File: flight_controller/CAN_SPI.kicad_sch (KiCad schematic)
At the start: 11 parts, among them CN2 HCZZ0494-4, CN3 HCZZ0494-4, U3 TJA1051TK/3,118, U5 TJA1051TK/3,118, U6 KRCLAMP0521P-N

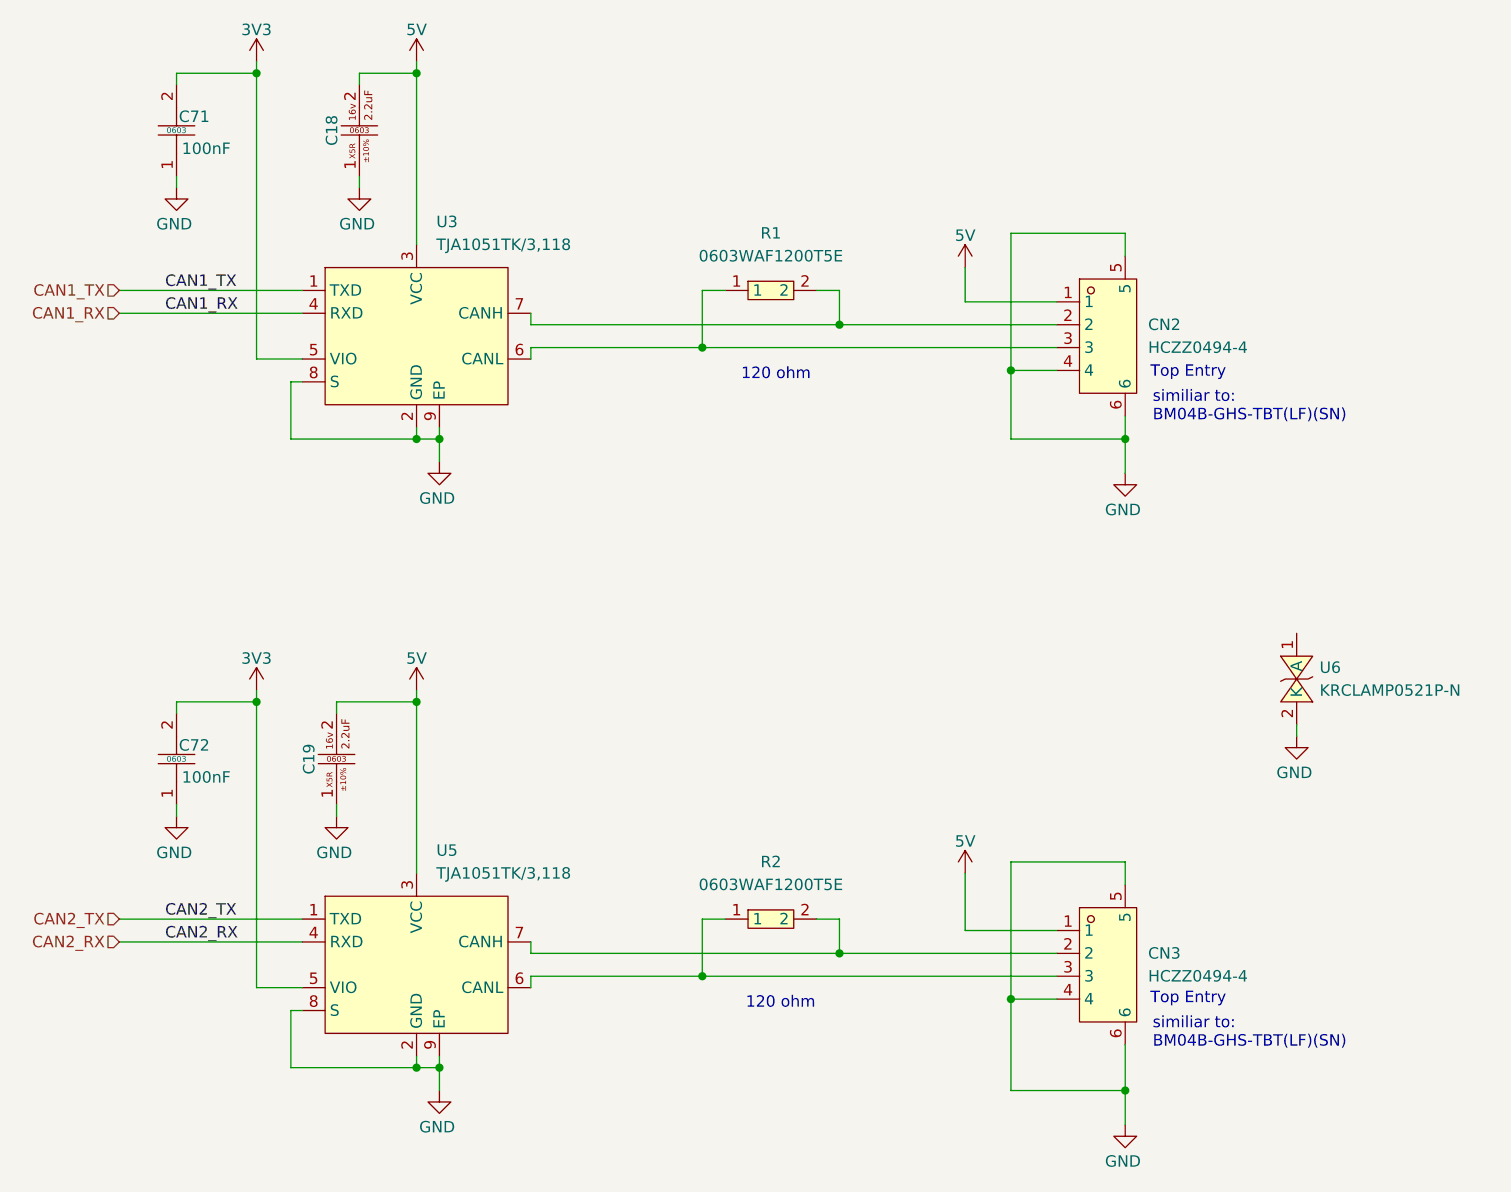
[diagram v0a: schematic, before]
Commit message: updating symbols as in the shared library
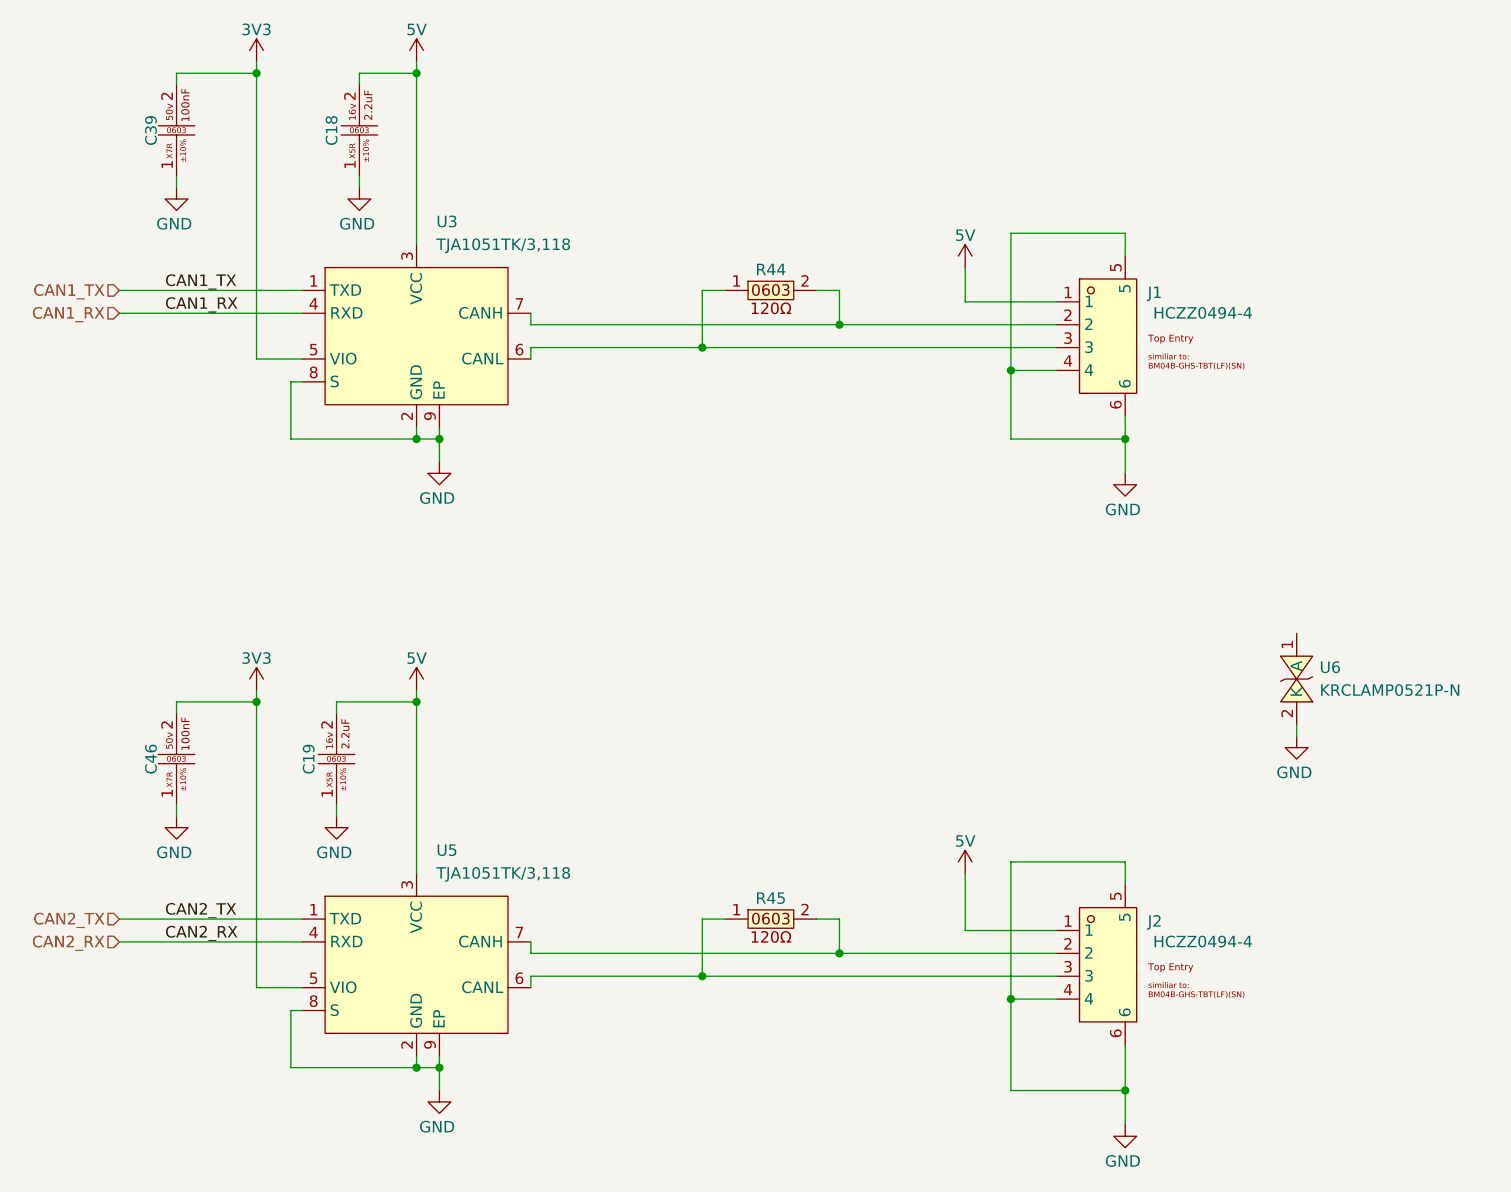
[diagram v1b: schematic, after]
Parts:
- removed C71, C72: CC0603KRX7R9BB104, easyeda2kicad:C0603, symbol easyeda2kicad:CC0603KRX7R9BB104
- removed CN2, CN3: HCZZ0494-4, easyeda2kicad:CONN-SMD_4P-P1.25_BM04B-GHS-TBT-LF-SN, symbol lampelKicadLIB:HCZZ0494-4
- removed R1, R2: 0603WAF1200T5E, easyeda2kicad:R0603, symbol lampelKicadLIB:0603WAF1200T5E
- added C39, C46: CC0603KRX7R9BB104 (100nf , 0603 ,50v ,X7R), easyeda2kicad:C0603, symbol lampelKicadLIB:CC0603KRX7R9BB104 (100nf , 0603 ,50v ,X7R)
- added J1, J2: HCZZ0494-4, easyeda2kicad:CONN-SMD_4P-P1.25_BM04B-GHS-TBT-LF-SN, symbol lampelKicadLIB:HCZZ0494-4
- added R44, R45: 603WAF1200T5E, easyeda2kicad:R0603, symbol lampelKicadLIB:0603WAF1200T5E (120ohm,0603)
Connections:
- net 3V3: now also C39.2, C46.2
- net 5V: now also J1.1, J2.1
- net GND: now also C39.1, C46.1, J1.4, J1.5, J1.6, J2.4, J2.5, J2.6
- net at U5.6 (CANL): now also J2.3, R45.1
- net at U5.7 (CANH): now also J2.2, R45.2
- net at U3.7 (CANH): now also J1.2, R44.2
- net at U3.6 (CANL): now also J1.3, R44.1
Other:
- note removed: "120 ohm"
- note removed: "Top Entry"
- note removed: "similiar to: BM04B-GHS-TBT(LF)(SN)"

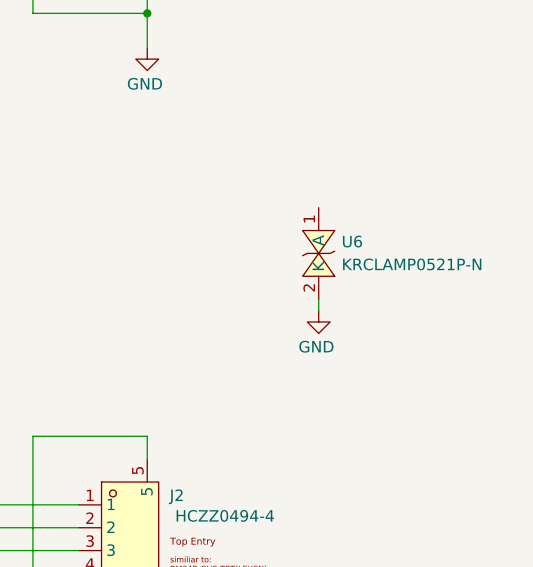
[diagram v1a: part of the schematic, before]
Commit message: update debug conn
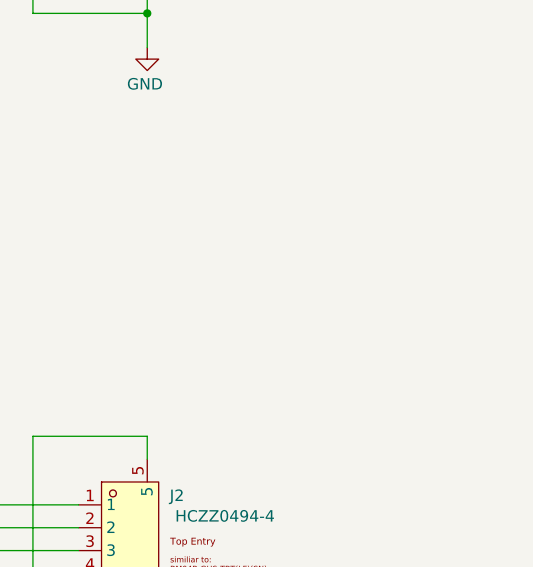
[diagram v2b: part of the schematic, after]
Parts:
- removed U6: KRCLAMP0521P-N, easyeda2kicad:DFN1006-2L-BI, symbol easyeda2kicad:KRCLAMP0521P-N
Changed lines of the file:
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@@
-	(wire
-		(pts
-			(xy 554.99 110.49) (xy 554.99 111.76)
-		)
-		(stroke
-			(width 0)
-			(type default)
-		)
-	)
 	(wire
 		(pts
@@
 	)
 	(symbol
-		(lib_id "power:GND")
-		(at 554.99 111.76 0)
-		(mirror y)
-		(unit 1)
-		(exclude_from_sim no)
-		(in_bom yes)
-		(on_board yes)
-		(dnp no)
-		(property "Reference" "#PWR078"
-			(at 554.99 118.11 0)
-			(effects
-				(font
-					(size 1.27 1.27)
-				)
-				(hide yes)
-			)
-		)
-		(property "Value" "GND"
-			(at 554.736 115.824 0)
-			(effects
-				(font
-					(size 1.27 1.27)
-				)
-			)
-		)
-		(property "Footprint" ""
-			(at 554.99 111.76 0)
-			(effects
-				(font
-					(size 1.27 1.27)
-				)
-				(hide yes)
-			)
-		)
-		(property "Datasheet" ""
-			(at 554.99 111.76 0)
-			(effects
-				(font
-					(size 1.27 1.27)
-				)
-				(hide yes)
-			)
-		)
-		(property "Description" "Power symbol creates a global label with name \"GND\" , ground"
-			(at 554.99 111.76 0)
-			(effects
-				(font
-					(size 1.27 1.27)
-				)
-				(hide yes)
-			)
-		)
-		(pin "1"
-		)
-		(instances
-			(project "FP_BOARD"
-				(path "/17737359-1a8e-4237-8899-d9604030bc1d/bc534bd1-f491-4966-ba4f-9fc6d85cb066"
-					(reference "#PWR078")
-					(unit 1)
-				)
-			)
-		)
-	)
-	(symbol
 		(lib_id "power:VDD")
 		(at 518.16 127 0)
@@
 					(unit 1)
 				)
-			)
-		)
-	)
-	(symbol
-		(lib_id "easyeda2kicad:KRCLAMP0521P-N")
-		(at 554.99 105.41 90)
-		(unit 1)
-		(exclude_from_sim no)
-		(in_bom yes)
-		(on_board yes)
-		(dnp no)
-		(fields_autoplaced yes)
-		(property "Reference" "U6"
-			(at 557.53 104.1399 90)
-			(effects
-				(font
-					(size 1.27 1.27)
-				)
-				(justify right)
-			)
-		)
-		(property "Value" "KRCLAMP0521P-N"
-			(at 557.53 106.6799 90)
-			(effects
-				(font
-					(size 1.27 1.27)
-				)
-				(justify right)
-			)
-		)
-		(property "Footprint" "easyeda2kicad:DFN1006-2L-BI"
-			(at 562.61 105.41 0)
-			(effects
-				(font
-					(size 1.27 1.27)
-				)
-				(hide yes)
-			)
-		)
-		(property "Datasheet" ""
-			(at 554.99 105.41 0)
-			(effects
-				(font
-					(size 1.27 1.27)
-				)
-				(hide yes)
-			)
-		)
-		(property "Description" ""
-			(at 554.99 105.41 0)
-			(effects
-				(font
-					(size 1.27 1.27)
-				)
-				(hide yes)
-			)
-		)
-		(property "LCSC Part" "C2985618"
-			(at 565.15 105.41 0)
-			(effects
-				(font
-					(size 1.27 1.27)
-				)
-				(hide yes)
-			)
-		)
-		(pin "1"
-		)
-		(pin "2"
-		)
-		(instances
-			(project "FP_BOARD"
-				(path "/17737359-1a8e-4237-8899-d9604030bc1d/bc534bd1-f491-4966-ba4f-9fc6d85cb066"
-					(reference "U6")
-					(unit 1)
-				)

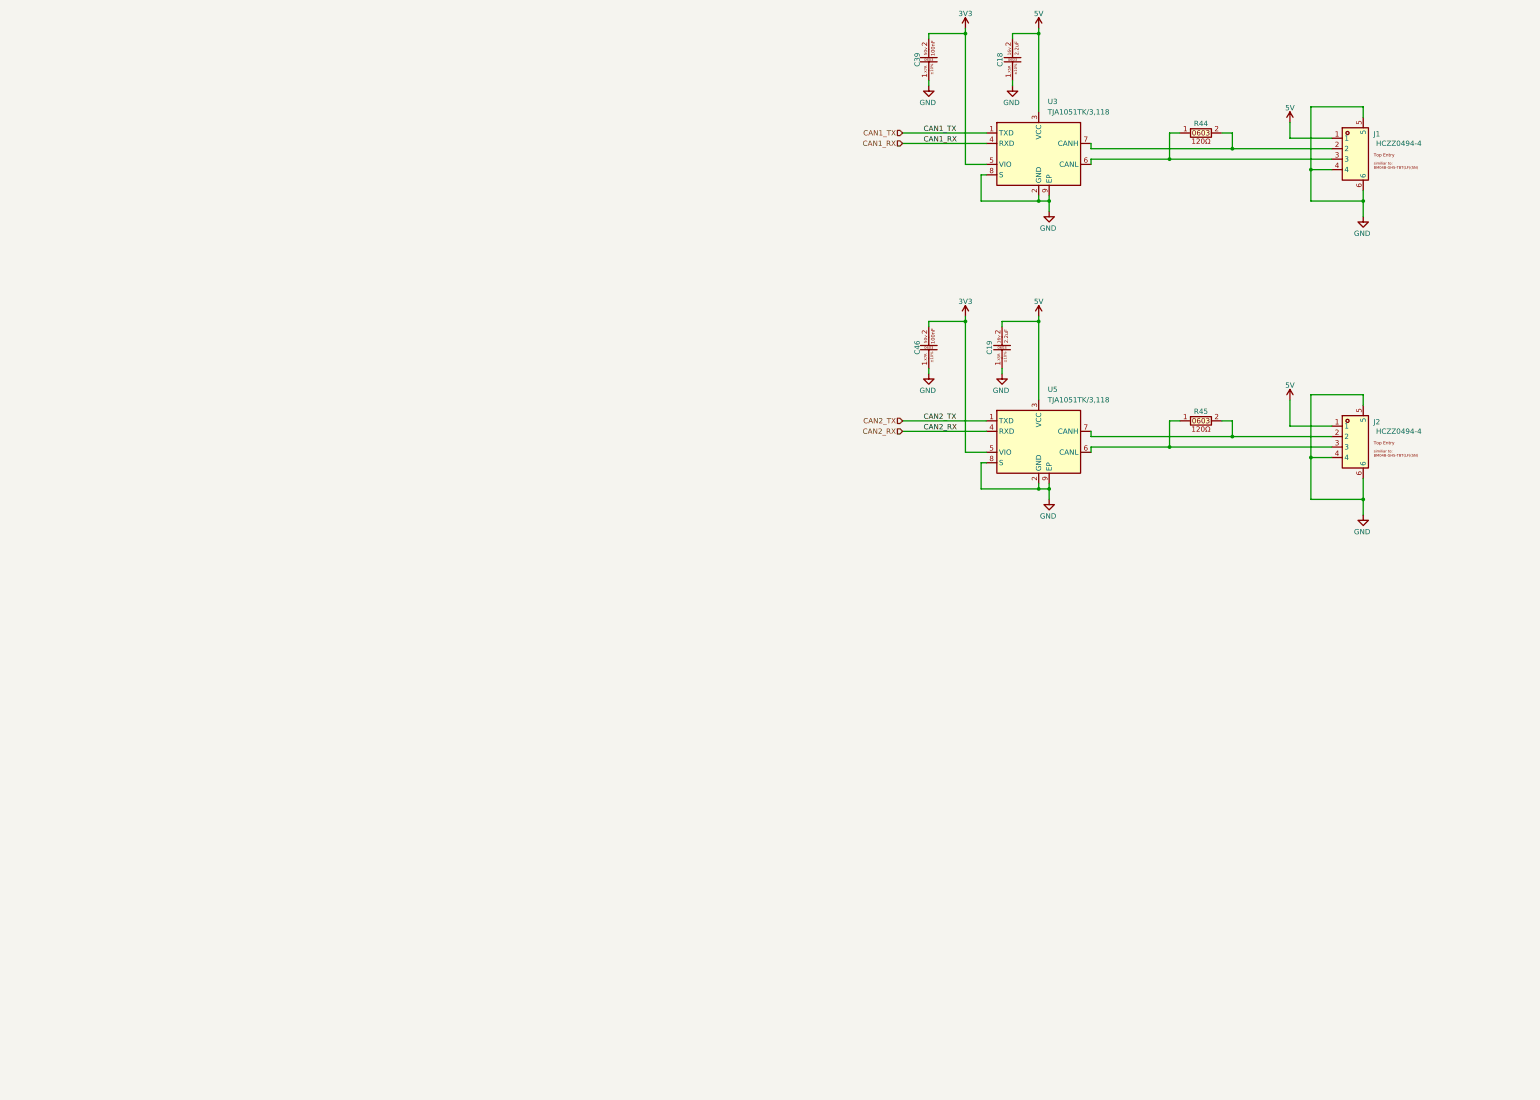
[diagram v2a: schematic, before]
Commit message: ALL CONNECTORS, ETH, SERVO,RC,SPI,FLASH and more. to finish GPSand STM32 PINOUT
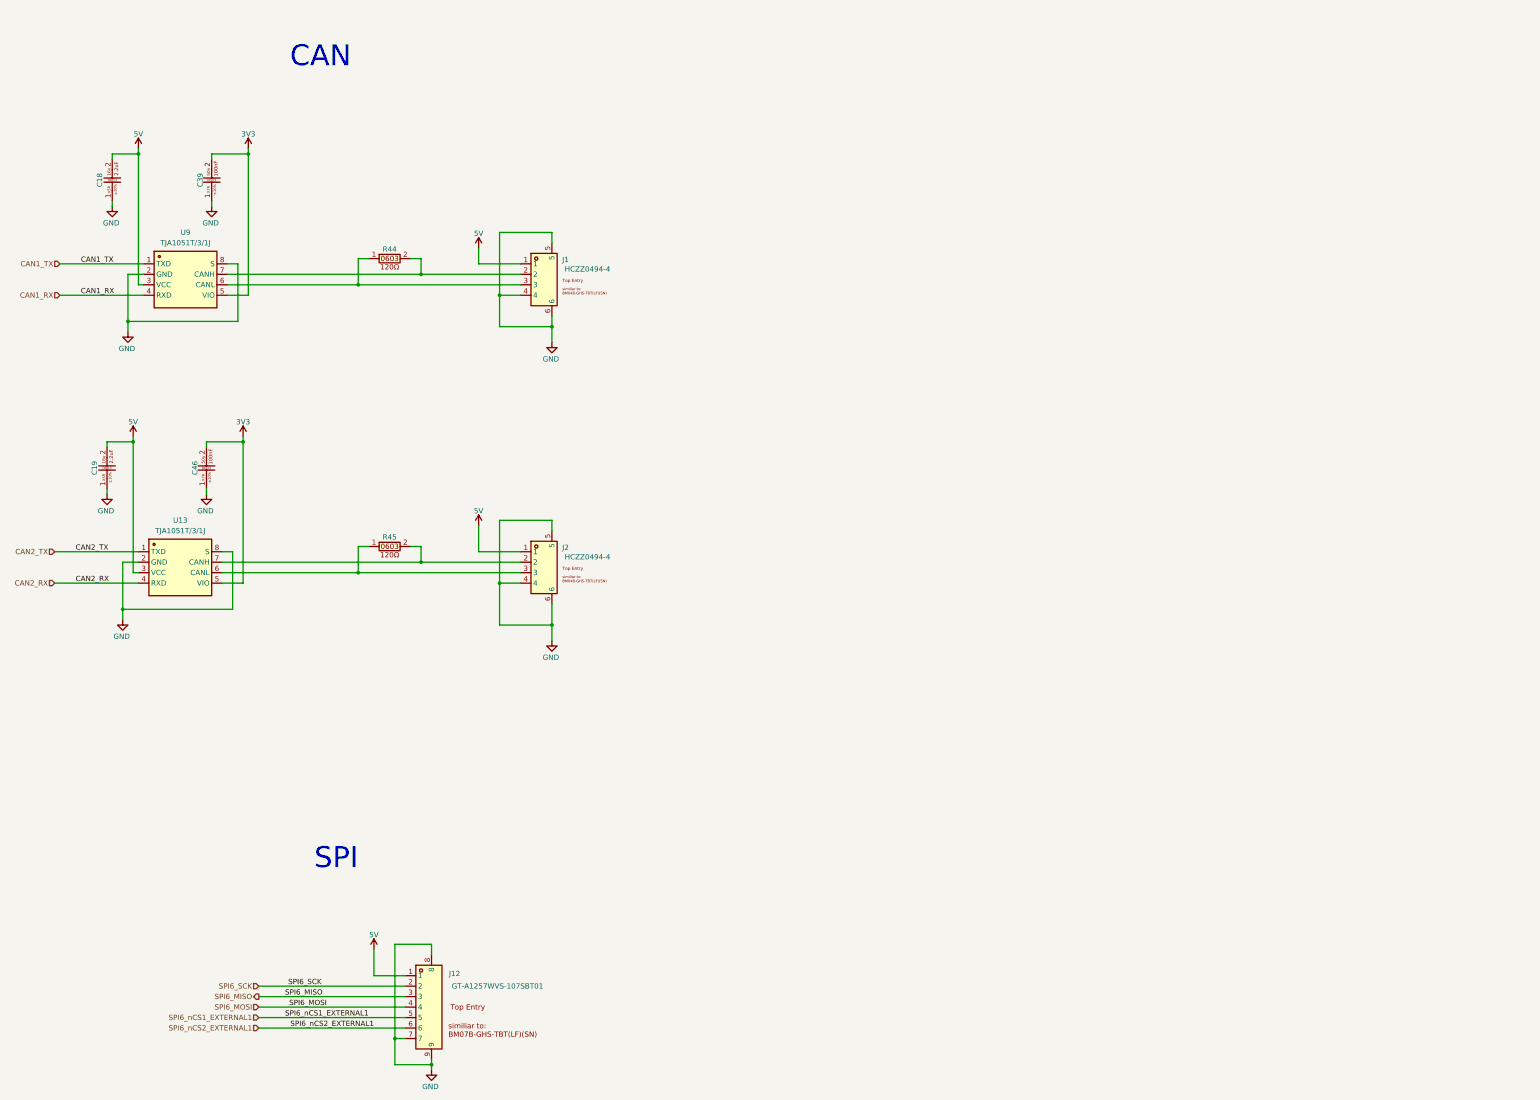
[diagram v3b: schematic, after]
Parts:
- removed U3, U5: TJA1051TK/3,118, easyeda2kicad:HVSON-8_L3.0-W3.0-P0.65-BL-EP, symbol easyeda2kicad:TJA1051TK_3,118
- added J12: GT-A1257WVS-107SBT01, easyeda2kicad:CONN-SMD_7P-P1.25_BM07B-GHS-TBT-LF-SN-N, symbol lampelKicadLIB:GT-A1257WVS-107SBT01
- added U13, U9: TJA1051T/3/1J, easyeda2kicad:SOIC-8_L4.9-W3.9-P1.27-LS6.0-BL, symbol lampelKicadLIB:TJA1051T_3_1J
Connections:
- net 3V3: now also U13.5 (VIO), U9.5 (VIO)
- net 5V: now also J12.1, U13.3 (VCC), U9.3 (VCC)
- net CAN1_RX: now also U9.4 (RXD)
- net CAN1_TX: now also U9.1 (TXD)
- net CAN2_RX: now also U13.4 (RXD)
- net CAN2_TX: now also U13.1 (TXD)
- net GND: now also J12.7, J12.8, J12.9, U13.2 (GND), U13.8 (S), U9.2 (GND), U9.8 (S)
- net at J2.2, R45.2: now also U13.7 (CANH)
- net at J2.3, R45.1: now also U13.6 (CANL)
- net at J1.3, R44.1: now also U9.6 (CANL)
- net at J1.2, R44.2: now also U9.7 (CANH)
- new net SPI6_MISO: J12.3
- new net SPI6_MOSI: J12.4
- new net SPI6_SCK: J12.2
- new net SPI6_nCS1_EXTERNAL1: J12.5
- new net SPI6_nCS2_EXTERNAL1: J12.6
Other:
- note added: "CAN"
- note added: "SPI"
- moved on the sheet: C18, C39, J1, J2, R44, R45

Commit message: cleanup and improvements
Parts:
- removed J12: GT-A1257WVS-107SBT01, easyeda2kicad:CONN-SMD_7P-P1.25_BM07B-GHS-TBT-LF-SN-N, symbol lampelKicadLIB:GT-A1257WVS-107SBT01
- added C74: CC0603KRX7R9BB104 (100nf , 0603 ,50v ,X7R), easyeda2kicad:C0603, symbol lampelKicadLIB:CC0603KRX7R9BB104 (100nf , 0603 ,50v ,X7R)
- added J18: A1257WV-S-6P-LCP, easyeda2kicad:CONN-SMD_A1257WV-S-6P, symbol lampelKicadLIB:A1257WV-S-6P-LCP
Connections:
- net 5V: now also C74.2, J18.1
- net GND: now also C74.1, J18.6, J18.7, J18.8
- new net SPI3_MISO: J18.3
- new net SPI3_MOSI: J18.4
- new net SPI3_SCK: J18.2
- new net SPI3_nCS1: J18.5
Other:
- note added: "SPI3 EXTERNAL"
- note removed: "SPI"
